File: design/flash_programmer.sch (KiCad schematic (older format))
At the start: 0 parts

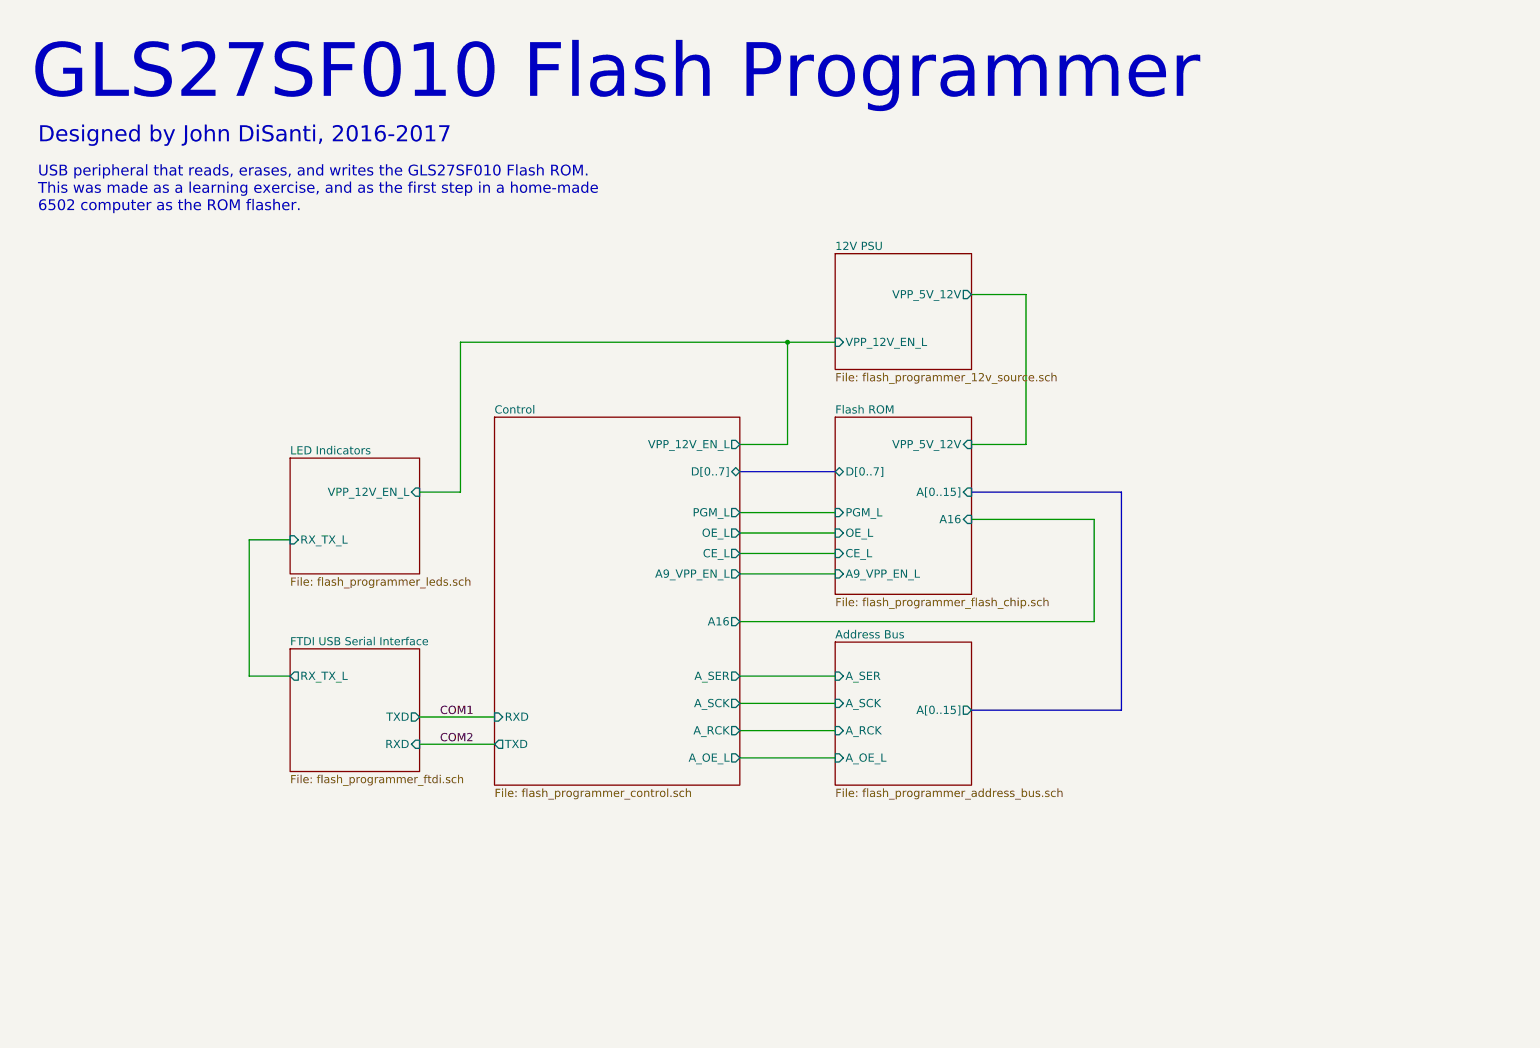
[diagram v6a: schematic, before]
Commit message: Apply license to schematic files
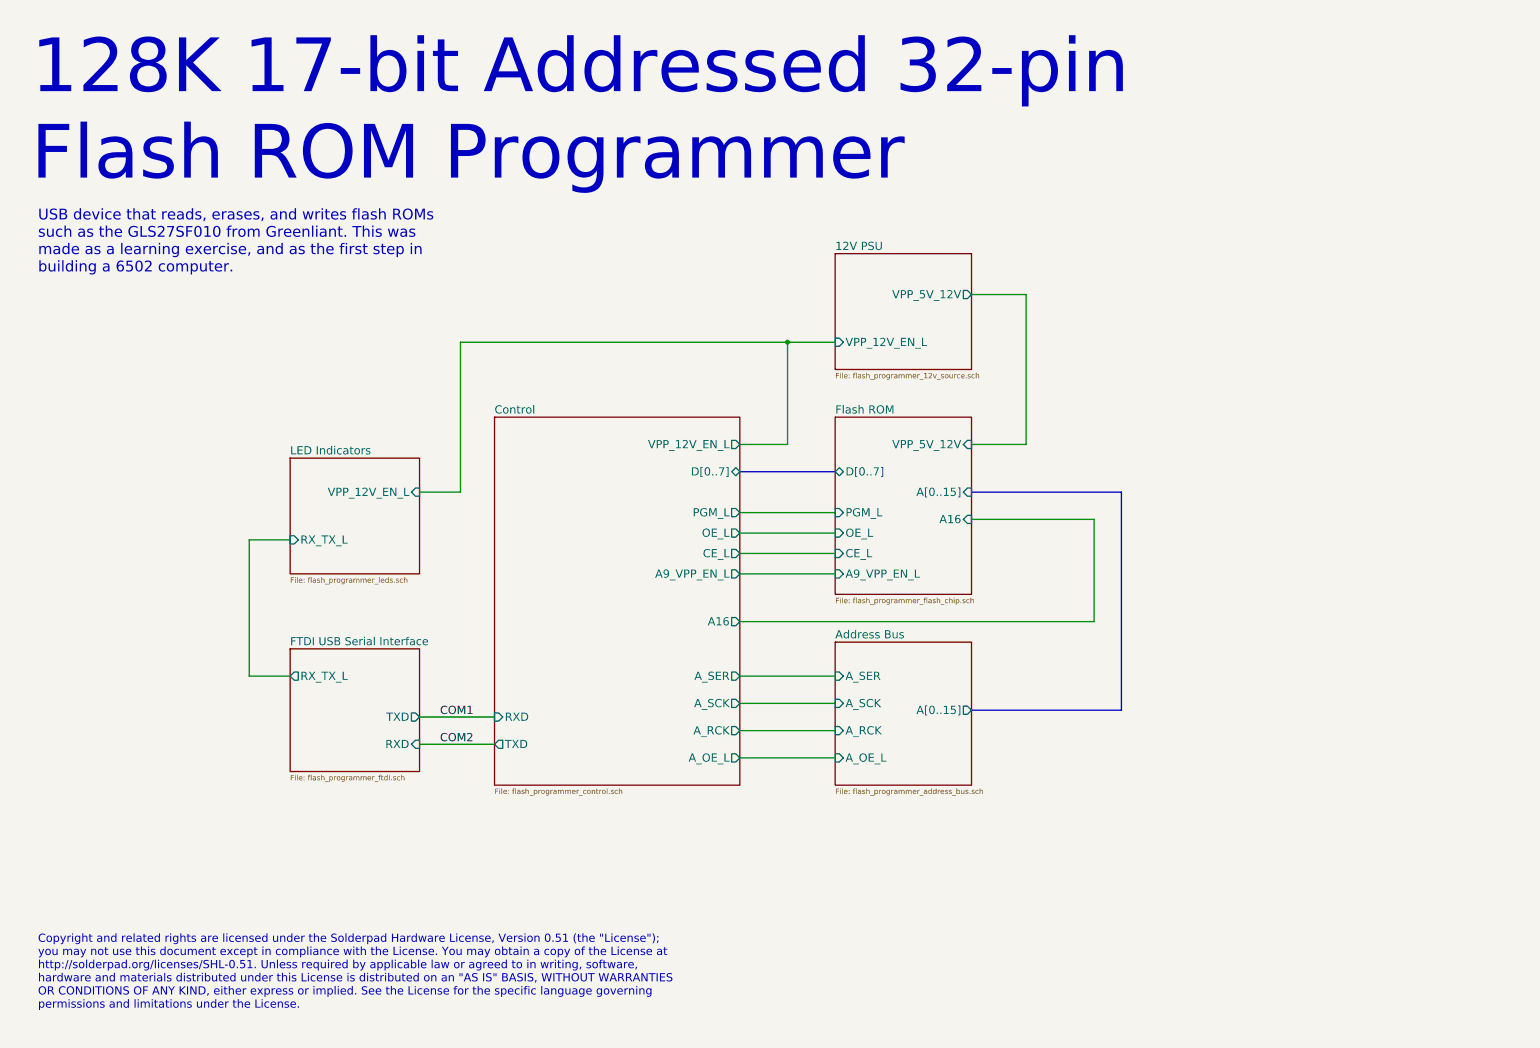
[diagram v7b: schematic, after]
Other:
- note added: "128K 17-bit Addressed 32-pin\nFlash ROM Programmer"
- note added: "Copyright and related rights are licensed under the Solderpad Hardware License, Version 0.51 (the "License");\nyou may not use this document except in compliance with the License. You may obtain a copy of the License at\nhttp://solderpad.org/licenses/SHL-0.51. Unless required by applicable law or agreed to in writing, software,\nhardware and materials distributed under this License is distributed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"
- note added: "USB device that reads, erases, and writes flash ROMs\nsuch as the GLS27SF010 from Greenliant. This was\nmade as a learning exercise, and as the first step in\nbuilding a 6502 computer."
- note removed: "Designed by John DiSanti, 2016-2017"
- note removed: "GLS27SF010 Flash Programmer"
- note removed: "USB peripheral that reads, erases, and writes the GLS27SF010 Flash ROM.\nThis was made as a learning exercise, and as the first step in a home-made\n6502 computer as the ROM flasher."
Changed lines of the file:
@@
 Date "2017-03-11"
 Rev "5"
-Comp "John DiSanti"
+Comp "Copyright 2017 John DiSanti"
 Comment1 ""
 Comment2 ""
@@
 U 58665314
 F0 "FTDI USB Serial Interface" 59
-F1 "flash_programmer_ftdi.sch" 59
+F1 "flash_programmer_ftdi.sch" 39
 F2 "RXD" I R 3500 5850 60
 F3 "TXD" O R 3500 5650 60
@@
 U 58BA78AE
 F0 "Flash ROM" 60
-F1 "flash_programmer_flash_chip.sch" 60
+F1 "flash_programmer_flash_chip.sch" 39
 F2 "OE_L" I L 6550 4300 60
 F3 "CE_L" I L 6550 4450 60
@@
 U 58C44875
 F0 "12V PSU" 60
-F1 "flash_programmer_12v_source.sch" 60
+F1 "flash_programmer_12v_source.sch" 39
 F2 "VPP_12V_EN_L" I L 6550 2900 60
 F3 "VPP_5V_12V" O R 7550 2550 60
@@
 Wire Wire Line
 	7950 3650 7550 3650
-Text Notes 650  1150 0    394  ~ 0
-GLS27SF010 Flash Programmer
-Text Notes 700  1450 0    118  ~ 0
-Designed by John DiSanti, 2016-2017
-Text Notes 700  1950 0    79   ~ 0
-USB peripheral that reads, erases, and writes the GLS27SF010 Flash ROM.\nThis was made as a learning exercise, and as the first step in a home-made\n6502 computer as the ROM flasher.
+Text Notes 650  1750 0    394  ~ 0
+128K 17-bit Addressed 32-pin\nFlash ROM Programmer
+Text Notes 700  2400 0    79   ~ 0
+USB device that reads, erases, and writes flash ROMs\nsuch as the GLS27SF010 from Greenliant. This was\nmade as a learning exercise, and as the first step in\nbuilding a 6502 computer.
 $Sheet
 S 6550 5100 1000 1050
 U 58C678D4
 F0 "Address Bus" 60
-F1 "flash_programmer_address_bus.sch" 60
+F1 "flash_programmer_address_bus.sch" 39
 F2 "A_SER" I L 6550 5350 60
 F3 "A_SCK" I L 6550 5550 60
@@
 U 58C243E5
 F0 "Control" 60
-F1 "flash_programmer_control.sch" 60
+F1 "flash_programmer_control.sch" 39
 F2 "RXD" I L 4050 5650 60
 F3 "PGM_L" O R 5850 4150 60
@@
 U 58C7589B
 F0 "LED Indicators" 60
-F1 "flash_programmer_leds.sch" 60
+F1 "flash_programmer_leds.sch" 39
 F2 "VPP_12V_EN_L" I R 3500 4000 60
 F3 "RX_TX_L" I L 2550 4350 60
@@
 Wire Wire Line
 	8450 4200 7550 4200
+Text Notes 700  7800 0    60   ~ 0
+Copyright and related rights are licensed under the Solderpad Hardware License, Version 0.51 (the "License");\nyou may not use this document except in compliance with the License. You may obtain a copy of the License at\nhttp://solderpad.org/licenses/SHL-0.51. Unless required by applicable law or agreed to in writing, software,\nhardware and materials distributed under this License is distributed on an "AS IS" BASIS, WITHOUT WARRANTIES\nOR CONDITIONS OF ANY KIND, either express or implied. See the License for the specific language governing\npermissions and limitations under the License.
 $EndSCHEMATC
